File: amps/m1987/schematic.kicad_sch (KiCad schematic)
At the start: 75 parts, among them T1 OT

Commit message: Add: real tube pin numbers and readable valve glyphs on every schematic
Phase B of the drawing program. A factory service sheet numbers every tube
pin, because the number is what a technician puts a probe on. This corpus
printed none, and the numbers hidden in its symbols were positional
placeholders (P=1, G=2, K=3) that would have published a 6V6GT's plate as
pin 1 when it is pin 3.

1055 electrodes now carry the real number, 1027 lettered (27 are shared
filaments deduped, 1 dropped for want of clear space on the 6G2). Resolved per
instance from reference/tubes/<slug>.yaml through the same alias resolution the
layout renderer uses, so a 12AX7 section and a 6SL7 section each get their own
basing. A valve whose basing the corpus does not carry prints nothing rather
than a wrong number.

Section letters and basing units are now separate things, which cost a detour
worth recording. The RCA 12AX7-A sheet reads "Pin 1 - Plate of Unit No.2 ...
Pin 6 - Plate of Unit No.1", so unit numbering is not pin order; the 5Y3 and
GZ34 number their units in opposite pin order, so nothing positional can
express it. But the section LETTER is a designator, not a basing fact: this
corpus, like every technician, calls the first stage in signal order V1A, and
five amps' prose already did. On four amps the factory sheets put that first
stage on the other half -- the AA764's own schematic prints +200 V on pin 1 --
so those drawings now state their unit explicitly, each citing its source, and
no letter, netlist, parts list or layout comment changed. 183 layout comments
agree with the printed numbers, 0 disagree. A guard fires if two halves of one
bottle resolve to the same unit, which is exactly how this was found.

Glyphs: the cathode gains a bracket and filament hairpin so it can no longer be
confused with the plate bar, the pentode's screen sits on its own row, and a
rectifier draws as one envelope over its sections instead of two apparent
bottles. Line weights are scaled per sheet to a co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
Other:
- note added: "1"
- note added: "2"
- note added: "3"
- note added: "4"
- note added: "5"
- note added: "6"
- note added: "7"
- note added: "8"

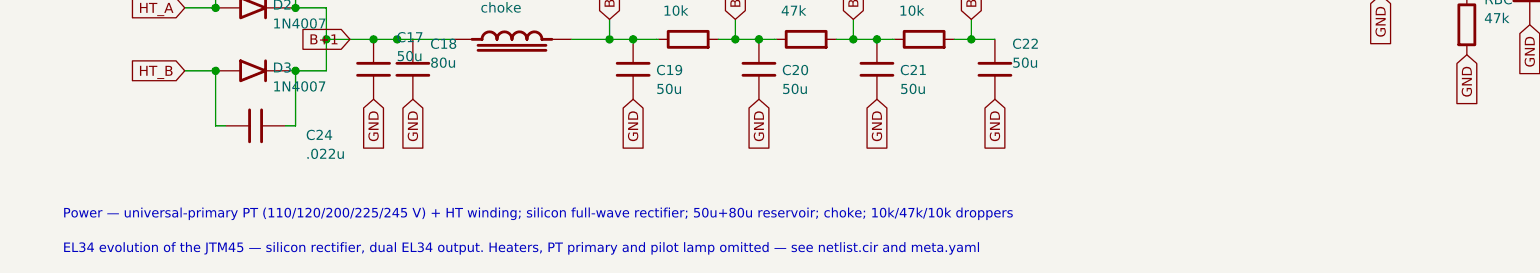
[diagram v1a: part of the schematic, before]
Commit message: Fix: schematic sheet notes no longer name repository files
Thirty-seven committed sheets rendered footnotes and section notes such as
"Heaters and PT primary omitted — see netlist.cir and meta.yaml" or
"excluded from netlist.cir (notes.md)" to visitors through KiCanvas. The
prose sweeps never counted sheets. Rewritten in the site's own words — the
netlist, the sources list, the circuit story, the parts list, the board
drawing — in 59 strings across 33 draw scripts, keeping every technical
claim as it was; the three tone sheets (6G4, 6G5, 6G6-B) are under repair
elsewhere and keep theirs for now. The sweep touched only strings passed to
the sheet's note, text, caption and footnote calls, never a path or a value.

Gates: check_schematics 40/0, connectivity 0 isolated pins;
verify_schematic_nets 40 clean; only the regenerated sheets and their served
copies changed.

Co-Authored-By: Claude Fable 5.1 <noreply@anthropic.com>
Claude-Session: https://claude.ai/code/session_01KBMfdh37HmCL2iWcBiL5J1
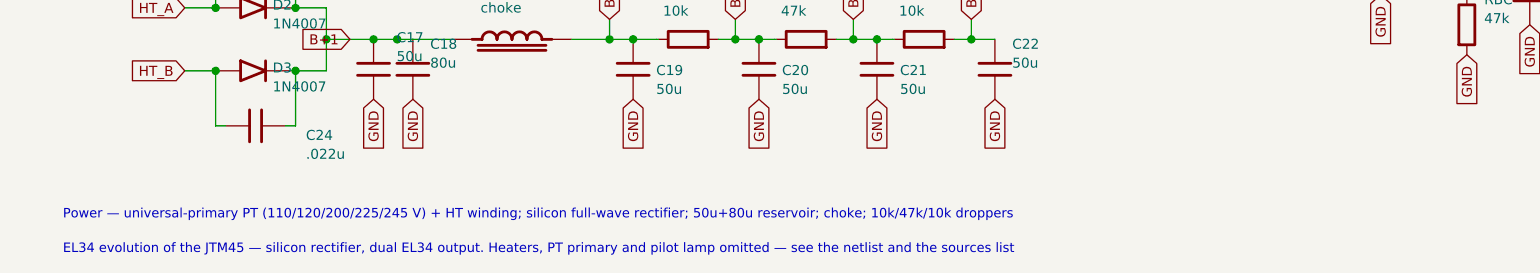
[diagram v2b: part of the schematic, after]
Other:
- note added: "EL34 evolution of the JTM45 — silicon rectifier, dual EL34 output. Heaters, PT primary and pilot lamp omitted — see the netlist and the sources list"
- note removed: "EL34 evolution of the JTM45 — silicon rectifier, dual EL34 output. Heaters, PT primary and pilot lamp omitted — see netlist.cir and meta.yaml"
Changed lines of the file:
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@@
   (text "Power — universal-primary PT (110/120/200/225/245 V) + HT winding; silicon full-wave rectifier; 50u+80u reservoir; choke; 10k/47k/10k droppers" (at 12.7 146.018 0)
     (effects (font (size 1.2 1.2)) (justify left)))
-  (text "EL34 evolution of the JTM45 — silicon rectifier, dual EL34 output. Heaters, PT primary and pilot lamp omitted — see netlist.cir and meta.yaml" (at 12.7 150.418 0)
+  (text "EL34 evolution of the JTM45 — silicon rectifier, dual EL34 output. Heaters, PT primary and pilot lamp omitted — see the netlist and the sources list" (at 12.7 150.418 0)
     (effects (font (size 1.2 1.2)) (justify left)))
   (sheet_instances (path "/" (page "1")))

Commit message: Fix: four single-sheet faults — 5G9 oscillator cathode grounded, B15N R36 bridging both rectifier plates, M1959/M1987 bias series resistor drawn as a shunt / after the diode
- 5g9: the factory sheet (crop 5g9-V3-schem.png) prints the oscillator
  cathode at +1.7 V on 1500 ‖ 25 µF, with the ladder's second 1M returned
  to that cathode node. The sheet had the same parts, but R7's ground flag
  stood ON the wire that returns R8 to the cathode, which grounded the
  whole node: RK3, CK3 and R8 all reported "the sheet shorts its two ends
  onto one net". The flag now points left from a shorter stub, clear of
  that wire. No part added — bom.yaml already carried RK3/CK3/R8.
- b15n: the Ampeg 591722 sheet (crop b15n-V6-rect.png, re-read at native
  resolution: R36's lower lead HOPS the B+ and screen lines and lands on
  the R35/D1 node with a dot) hangs R36 100K/2W on the pin-4 RED HT end.
  The sheet's feed wire ran from V6A's plate stub straight across the top
  of V6B's, joining both HT ends into one net (the SPLIT finding). R36 now
  takes its own HTA label. Caption reworded to name pin 4.
- m1959: the Unicord 70-6-11 sheet (crops m1959-bias-series.png,
  m1959-psu.png) runs the HT winding's end through the 27K (22K annotated)
  IN SERIES into the 1008 diode; the sheet drew it as a shunt at the
  diode. RBA is now in series before D1; bom role and circuit story
  reworded. The brief's "C24 on the bias node" does not exist on this
  amp: its bias filters are C17/C18 on sheet and BOM alike, C24 is the PI
  filter on both. The C24 on a bias-diode node was the M1987's rectifier
  snubber (below).
- m1987: the Unicord 70-19-11 sheet (crops m1987-bias.png, m1987-psu.png)
  runs the winding end through 220K into the diode, then 8 µF / 15K; the
  sheet had the diode first and the 220K after it, so RBA and RBB shared
  a node. RBA now sits before D1; RBA and RBB are separated by the diode.
  C24 (the D3 snubber, per bom.yaml) stays on HT_B and no longer shares a
  node with the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
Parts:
- removed D1: 1N4007, symbol cx:DIODE_SS
- removed RBC: 47k, symbol cx:R
- added RBA: 220k, symbol cx:R
- added VR6: 25k adj, symbol cx:POT
- D1: renamed from RBA; value 220k -> 1N4007; symbol cx:R -> cx:DIODE_SS
- RBC: renamed from VR6; value 25k adj -> 47k; symbol cx:POT -> cx:R
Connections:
- net -BIAS: now also VR6.2 (W); no longer RBC.2 (W)
- net GND: now also RBC.2
- net HT_B: now also RBA.1
- net at D1.1 (A): now also RBA.2
- net at RBC.1: now also VR6.3; no longer RBB.2
- new net: RBB.2, VR6.1
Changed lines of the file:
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@@
   (global_label "HT_B" (shape input) (at 152.3 110.409 180)
     (effects (font (size 1.27 1.27)) (justify right)))
-  (wire (pts (xy 152.3 110.409) (xy 156.11 110.409))
+  (symbol (lib_id "cx:R") (at 157.7 110.409 90) (unit 1)
+    (in_bom yes) (on_board yes)
+    (property "Reference" "RBA" (at 154.5 104.409 270) (effects (font (size 1.27 1.27)) (justify left)))
+    (property "Value" "220k" (at 154.5 106.809 270) (effects (font (size 1.27 1.27)) (justify left))))
+  (wire (pts (xy 152.3 110.409) (xy 153.89 110.409))
     (stroke (width 0) (type default)))
-  (symbol (lib_id "cx:DIODE_SS") (at 161.19 110.409 0) (unit 1)
+  (wire (pts (xy 161.51 110.409) (xy 162.52 110.409))
+    (stroke (width 0) (type default)))
+  (symbol (lib_id "cx:DIODE_SS") (at 167.6 110.409 0) (unit 1)
     (in_bom yes) (on_board yes)
-    (property "Reference" "D1" (at 159.19 105.009 0) (effects (font (size 1.27 1.27)) (justify left)))
-    (property "Value" "1N4007" (at 159.19 107.409 0) (effects (font (size 1.27 1.27)) (justify left))))
-  (wire (pts (xy 166.27 110.409) (xy 170.08 110.409))
-    (stroke (width 0) (type default)))
-  (symbol (lib_id "cx:R") (at 173.89 110.409 90) (unit 1)
-    (in_bom yes) (on_board yes)
-    (property "Reference" "RBA" (at 170.69 104.409 270) (effects (font (size 1.27 1.27)) (justify left)))
-    (property "Value" "220k" (at 170.69 106.809 270) (effects (font (size 1.27 1.27)) (justify left))))
-  (wire (pts (xy 170.08 110.409) (xy 170.08 110.409))
-    (stroke (width 0) (type default)))
-  (wire (pts (xy 177.7 110.409) (xy 180.24 110.409))
+    (property "Reference" "D1" (at 165.6 105.009 0) (effects (font (size 1.27 1.27)) (justify left)))
+    (property "Value" "1N4007" (at 165.6 107.409 0) (effects (font (size 1.27 1.27)) (justify left))))
+  (wire (pts (xy 172.68 110.409) (xy 180.24 110.409))
     (stroke (width 0) (type default)))
   (junction (at 180.24 110.409) (diameter 1.056) (color 0 0 0 0))

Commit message: Fix: m1987 bias row drawn as 70-19-11 has it, D1 the right way round; C23/C24 on the HT winding; L1 value
- Sheet (claimed): the bias row starts at HT_A, the HT winding's switched
  top end (it started at HT_B), and runs the 220k in series into D1. D1 is
  now at rot 180 (label_rot 0): cathode toward the 220k, the AC side, anode on
  the first 8 uF. The polarity gate read the old D1 as REVERSED. The 15k feeds
  the bias node, which carries the second 8 uF, feeds both grid leaks as
  -BIAS, and is bled to ground through the 47k and the 25k trimmer drawn as a
  variable resistor; before, -BIAS was the trimmer's wiper. Source: 70-19-11
  at 2023 x 1304, crops (1250,480)-(1560,640) x4 and (1440,400)-(1560,500) x5.
- C23/C24: 0.22 uF from each HT end to the grounded centre tap, as the
  drawing places them (lettered 22 / .22; crop m1987-psu, 1400 x 1175). They
  were 0.022 uF across each diode. Changed on the sheet, in the BOM and on the
  board, which now places them beside D2/D3; the C2[34] not-drawn rule is gone.
- L1: BOM value 'inductance not printed'. The 0.5 A was the 1/2 A HT fuse's
  rating; 70-19-11 draws the choke unlettered (crop (1930,255)-(1995,340) x10).
  The board declares L1 not_on_board, as its siblings do for a choke stub.
- Board: cathode fields D1 a, D2 b, D3 b; T1.ct's approach moved clear of
  C24's ground eyelet.
- No sch_map change: -BIAS stays the grid-leak label net that the netlist's
  VBIAS drives. verify_schematic_nets m1987: PASS (CLAIMED).
- sheet-board m1987: MISPLACED 6 -> 0, SHEET-ONLY 1 -> 0, BOARD-ONLY 2 -> 2
  (RNFB/VRP, pre-existing).

Co-Authored-By: Claude Opus 5 (1M context) <noreply@anthropic.com>
Claude-Session: https://claude.ai/code/session_01KBMfdh37HmCL2iWcBiL5J1
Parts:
- removed C15: 8u, symbol cx:C
- removed D1: 1N4007, symbol cx:DIODE_SS
- removed L1: choke, symbol cx:CHOKE
- added C17, C22: 50u, symbol cx:C
- added RBA: 220k, symbol cx:R
- C15: renamed from RBA; value 220k -> 8u; symbol cx:R -> cx:C
- C23, C24: value .022u -> .22u
- D1: renamed from C22; value 50u -> 1N4007; symbol cx:C -> cx:DIODE_SS
- L1: renamed from C17; value 50u -> choke; symbol cx:C -> cx:CHOKE
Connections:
- net -BIAS: now also RBB.2, RBC.1; no longer VR6.2 (W)
- net B+1: now also C17.1; no longer C23.2, C24.2
- net B+2: now also L1.2
- net B+5: now also C22.1; no longer D1.1
- net GND: now also C15.2, C23.1, C24.2, VR6.3, C17.2, C22.2; no longer D1.2, L1.2, RBC.2
- net HT_A: now also C23.2, RBA.1; no longer C23.1
- net HT_B: no longer C15.1
- net at RBB.1: now also C15.1, D1.1 (A)
- net at VR6.1: now also RBC.2, VR6.2 (W); no longer RBB.2
- new net: D1.2 (K), RBA.2
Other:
- moved on the sheet: D1, RBC
